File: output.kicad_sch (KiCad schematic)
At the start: 17 parts, among them J1 Conn_01x03, U1 TPS563203

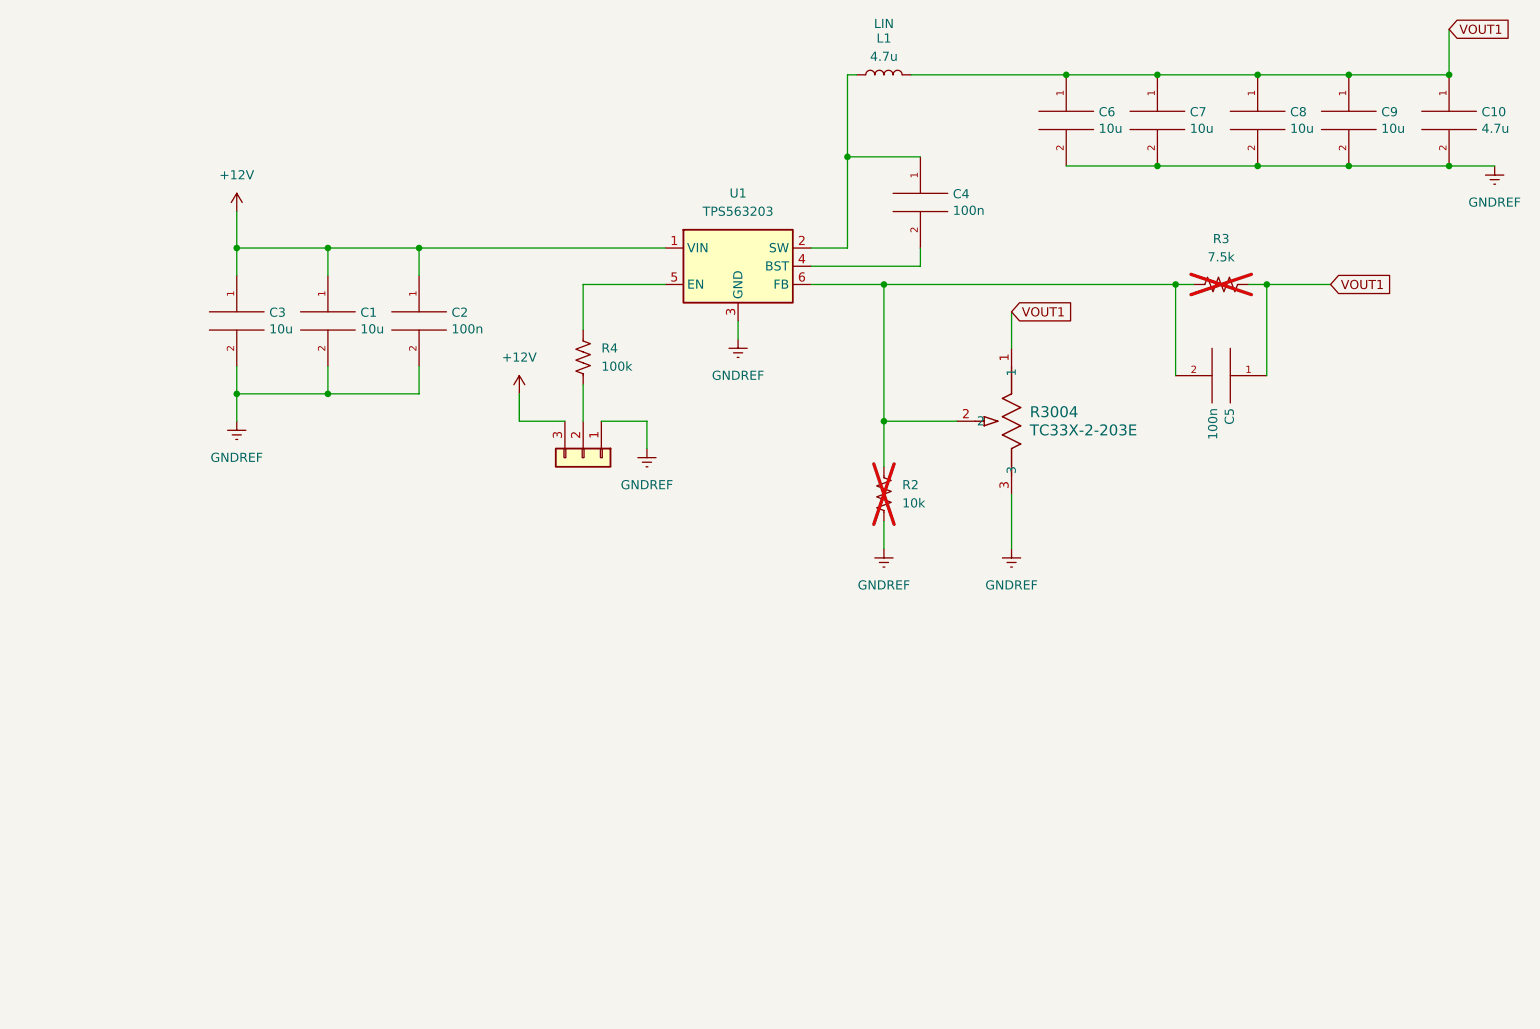
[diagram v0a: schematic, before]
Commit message: Added LEDs for status
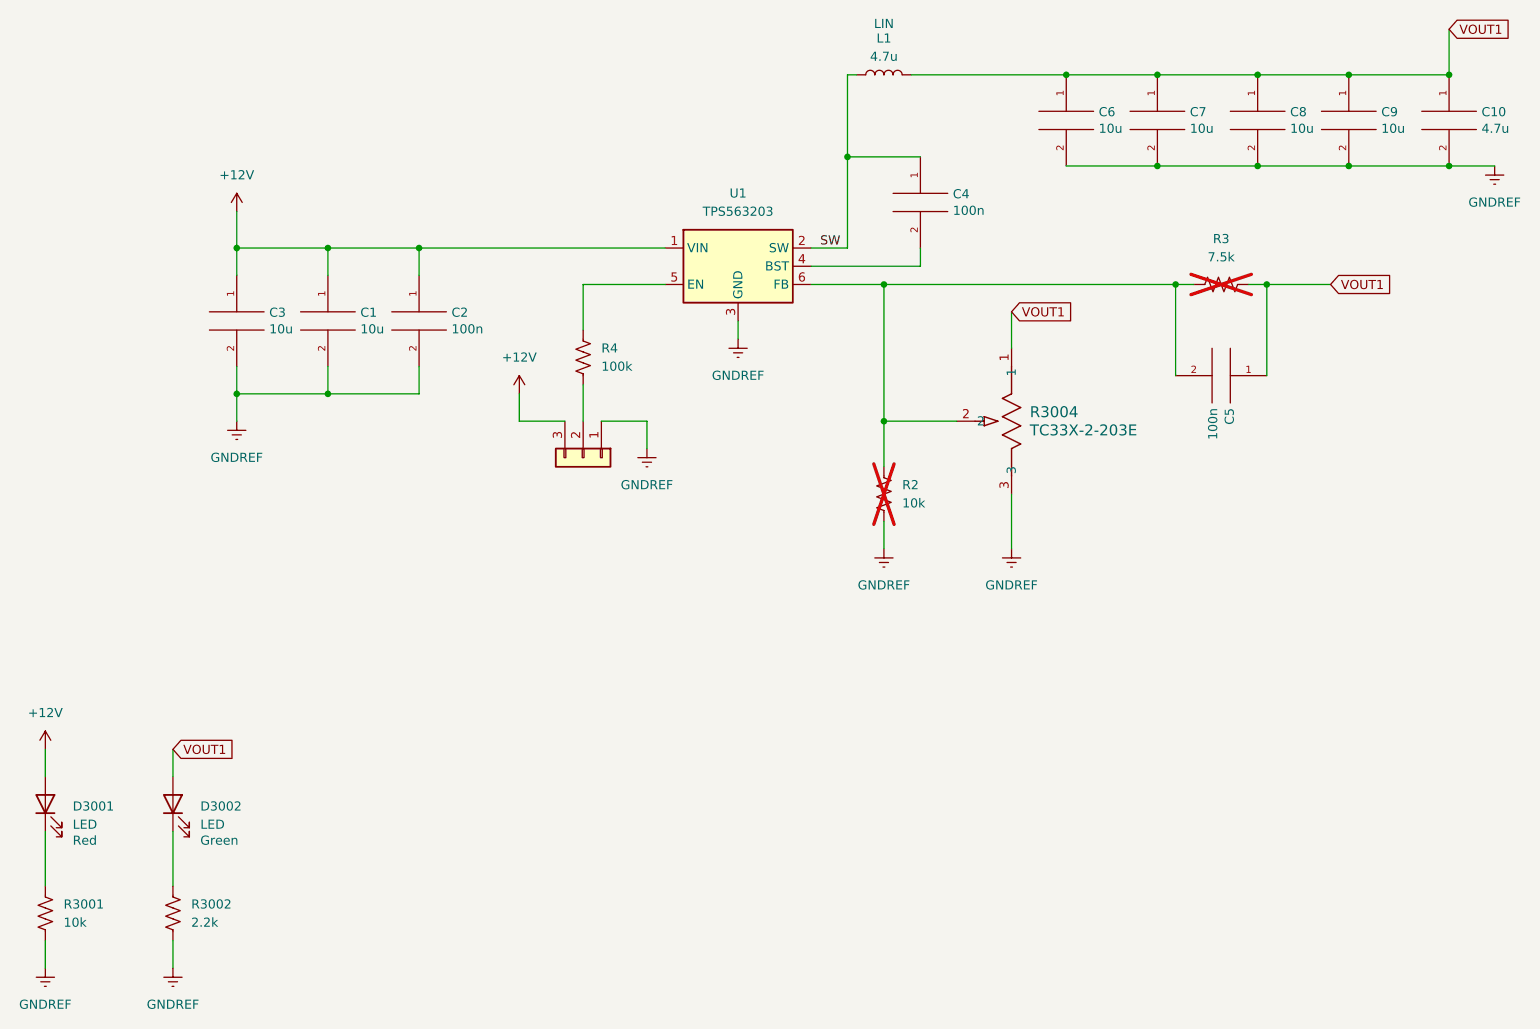
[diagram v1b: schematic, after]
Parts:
- added D3001, D3002: LED, LED_SMD:LED_0805_2012Metric, symbol Device:LED
- added R3001: 10k, Resistor_SMD:R_0805_2012Metric, symbol Device:R_US
- added R3002: 2.2k, Resistor_SMD:R_0805_2012Metric, symbol Device:R_US
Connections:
- net +12V: now also D3001.2 (A)
- net GNDREF: now also R3001.1, R3002.1
- net VOUT1: now also D3002.2 (A)
- net SW: now reaches C4.1, L1.1, U1.2 (SW)
- new net: D3001.1 (K), R3001.2
- new net: D3002.1 (K), R3002.2

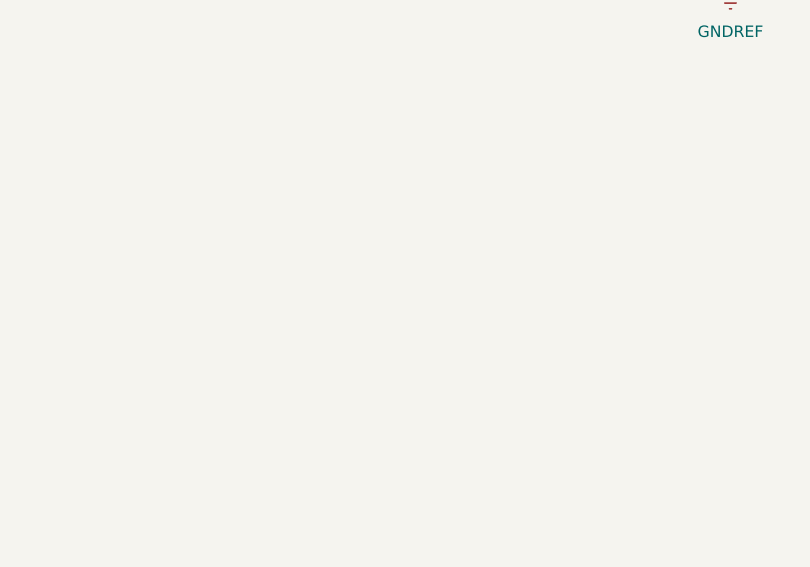
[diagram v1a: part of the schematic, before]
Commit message: Routing updates to ethernet
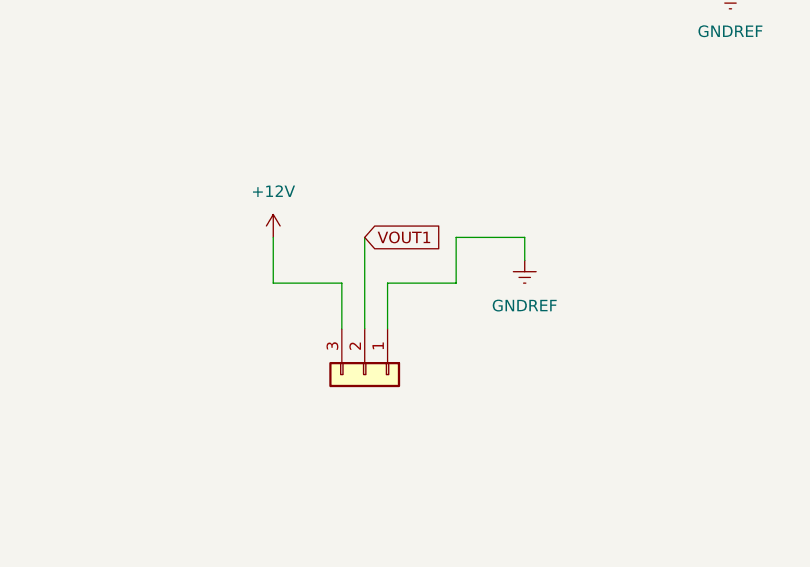
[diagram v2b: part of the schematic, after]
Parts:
- added J3001: Conn_01x03, SparkFun-Connector:1x03, symbol SparkFun-Connector:Conn_01x03
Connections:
- net +12V: now also J3001.3 (Pin_3)
- net GNDREF: now also J3001.1 (Pin_1)
- net VOUT1: now also J3001.2 (Pin_2)
